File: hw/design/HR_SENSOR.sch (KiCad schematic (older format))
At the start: 6 parts

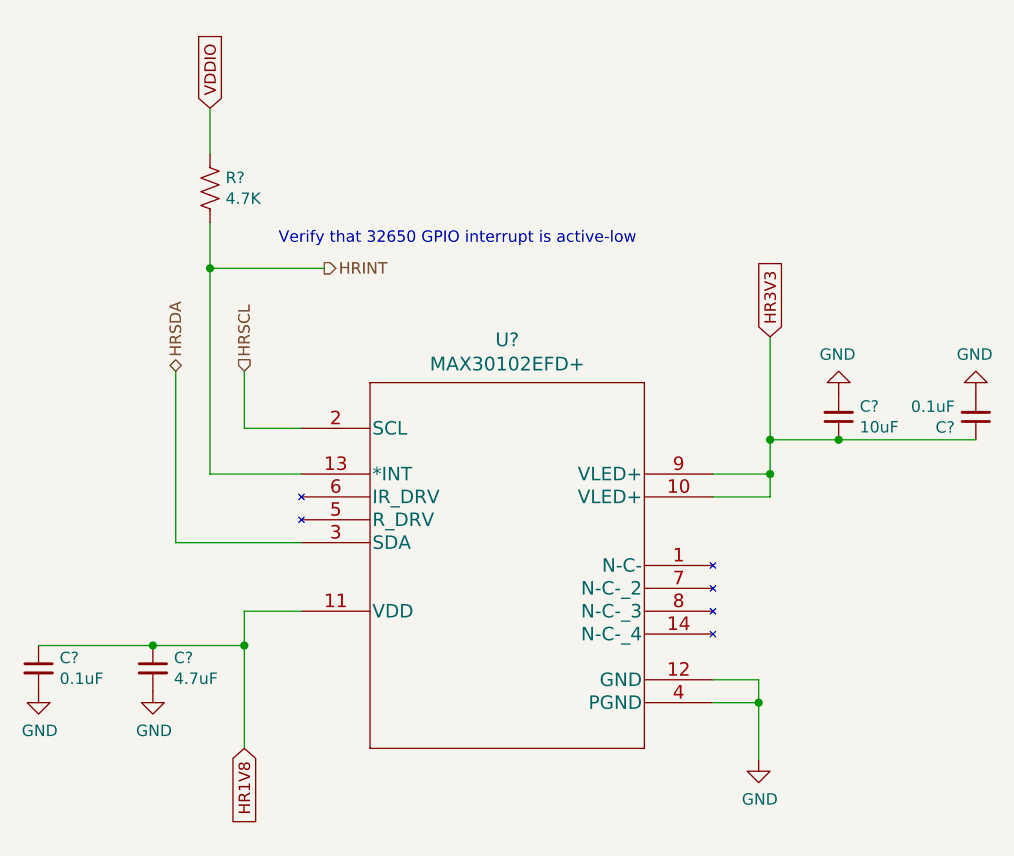
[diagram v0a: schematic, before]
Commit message: schematic/parts: SD Card
I have elected to move from writing notes to writing git commits instead. It may be easier to read for some.
Anyhow, I decided to research a little bit for a thinner SD card mount to improve my odds of the HR sensor being the tallest part on one side of the PCB.
Quite unlikely, but still. Didn't take much time at all and had to do some digging around for how the SD spec even works electronically.
Notes file will still keep track of all the parts, I might rename the file to "parts" as that's its most useful case other than me thinking on pixel.

Still workin'
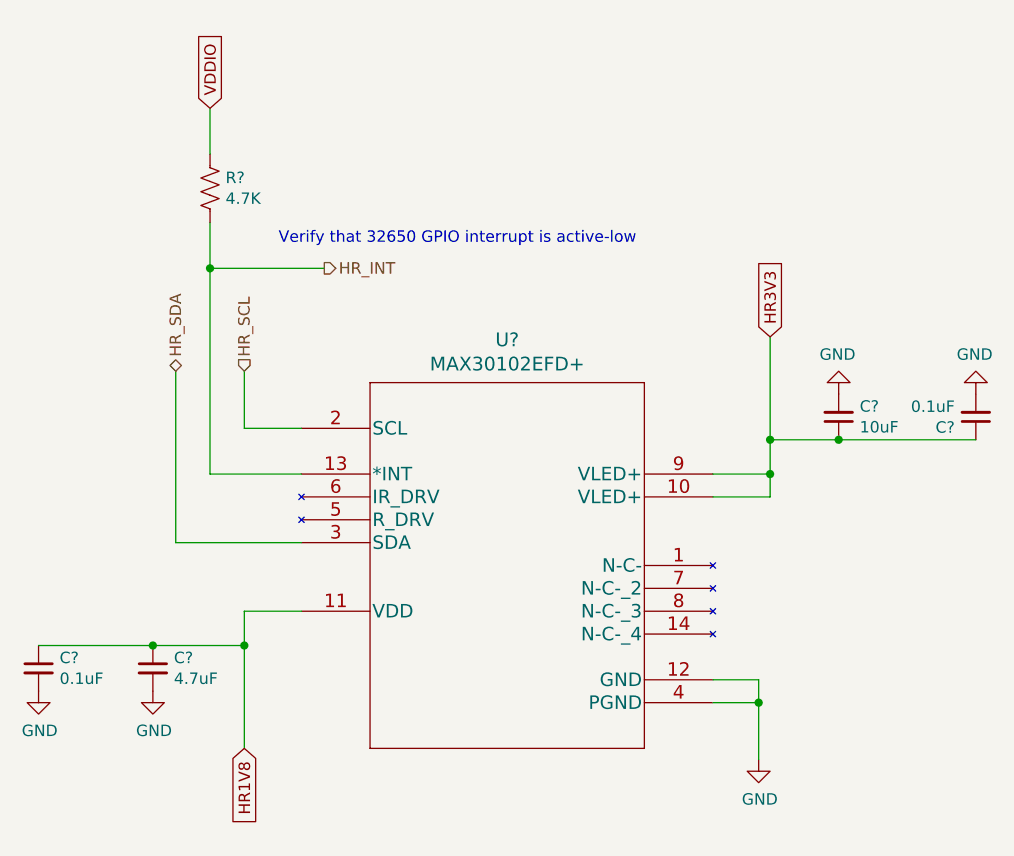
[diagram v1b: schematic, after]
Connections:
- net HRINT renamed HR_INT
- net HRSCL renamed HR_SCL
- net HRSDA renamed HR_SDA
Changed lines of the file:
@@
 $Descr A4 11693 8268
 encoding utf-8
-Sheet 2 5
+Sheet 2 6
 Title ""
 Date ""
@@
 Verify that 32650 GPIO interrupt is active-low
 Text HLabel 4400 3350 1    50   BiDi ~ 0
-HRSDA
+HR_SDA
 Text HLabel 4700 3350 1    50   Input ~ 0
-HRSCL
+HR_SCL
 Text HLabel 5050 2900 2    50   Output ~ 0
-HRINT
+HR_INT
 $EndSCHEMATC
